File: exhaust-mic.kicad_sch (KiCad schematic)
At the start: 0 parts

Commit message: modified:   01-power.kicad_sch 	modified:   02-analog.kicad_sch 	modified:   03-adc.kicad_sch 	modified:   04-mcu.kicad_sch 	modified:   05-io.kicad_sch 	new file:   exhaust-mic.kicad_pro 	modified:   exhaust-mic.kicad_sch 	modified:   mic-head/mic-head.kicad_pcb 	modified:   mic-head/mic-head.kicad_pro 	modified:   mic-head/mic-head.kicad_sch
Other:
- company: Hayabusa / exhaust-mic -> (none)
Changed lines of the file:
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@@
 		(title "Exhaust-Mic - Stereo-Tonaufnahme Motor und Auspuff")
 		(date "2026-08-28")
-		(rev "A")
-		(company "Hayabusa / exhaust-mic")
+		(rev "1")
 	)
 	(text "Auslegung, Rauschbudget und Pegelplan:"

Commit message: Layout verdrahten, ERC/DRC bereinigen, Werkzeugkette auf KiCad 10
Mikrofonkopf ist fertig verdrahtet (0 offene Verbindungen, 0 DRC-Fehler).
Auf der Hauptplatine bleiben 16 Verbindungen offen, ebenfalls ohne
DRC-Fehler; sie sind im interaktiven Router von KiCad zu schliessen.

Schaltplan
- 3 Speisepin-Fehler behoben (+4V6, ADC-AVDD, Uhrenbatterie brauchen ein
  Speiseflag - sie werden ueber Drossel, Ferrit bzw. Zelle gespeist und
  haben damit keine Quelle im Sinne der Regelpruefung)
- Netzname GND_CHASSIS entfernt: lag auf demselben Knoten wie GND
- TLV1117LV33 hatte einen Pin 4 fuer die Kuehlfahne, den es im Footprint
  SOT-223-3_TabPin2 nicht gibt - dort traegt Pad 2 die Fahne
- Piezo von Durchsteck- auf SMD-Ausfuehrung (Murata PKMCS0909E): fuer den
  12,5-mm-Typ gibt es keine Position, an der seine Anschluesse nicht auf
  der Gegenseite auf Pads treffen
- ERC laeuft jetzt fehlerfrei

Layout
- Durchsteckpads belegen beide Seiten. J1, J4 und J6 standen ueber
  rueckseitigen Bauteilen; das waren vier echte Kurzschluesse, unter
  anderem GPS_PPS gegen Masse an der Knopfzelle. Die eigene Pruefung
  vergleicht Durchsteckpads jetzt gegen beide Seiten, pad-genau
- In2 traegt keine Versorgungsinseln mehr, sondern Signale. Vorher wich
  der Autorouter auf die Masseflaeche aus - 140 Segmente aus 30 Netzen
  quer durch In1. Der DSN-Export kennzeichnet In1 nun als Versorgungslage
- Masseflaechen auf den Aussenlagen mit Naehvias an In1 angebunden und auf
  automatische Inselentfernung gestellt
- Netzklasse auf 0,18 mm Bahn, 0,15 mm Abstand, 0,5/0,25-mm-Via verengt;
  mit KiCads Vorgabewerten blieb rund ein Dutzend Verbindungen mehr offen
- Beschaffungsfelder unsichtbar und auf die Fab-Lage: sichtbar im
  Siebdruck ueberdecken die Herstellernummern die halbe Platine, das
  waren 151 der urspruenglich 214 Regelwarnungen

Werkzeuge
- pipeline.sh fasst den Layoutlauf zusammen
- fix_drc.py nimmt KiCads Regelpruefung als Instanz und entfernt, was sie
  beanstandet - die eigenen Abst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
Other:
- company: (none) -> Hayabusa / exhaust-mic
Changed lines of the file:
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@@
 		(title "Exhaust-Mic - Stereo-Tonaufnahme Motor und Auspuff")
 		(date "2026-08-28")
-		(rev "1")
+		(rev "A")
+		(company "Hayabusa / exhaust-mic")
 	)
 	(text "Auslegung, Rauschbudget und Pegelplan:"
@@
 		)
 	)
-	(embedded_fonts no)
 )

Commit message: modified:   01-power.kicad_sch 	modified:   02-analog.kicad_sch 	modified:   03-adc.kicad_sch 	modified:   04-mcu.kicad_sch 	modified:   05-io.kicad_sch 	modified:   exhaust-mic.kicad_pcb 	modified:   exhaust-mic.kicad_pro 	modified:   exhaust-mic.kicad_sch 	modified:   mic-head/mic-head.kicad_pcb 	modified:   mic-head/mic-head.kicad_pro 	modified:   mic-head/mic-head.kicad_sch 	new file:   ~exhaust-mic.kicad_pro.lck
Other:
- company: Hayabusa / exhaust-mic -> (none)
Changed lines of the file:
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@@
 		(title "Exhaust-Mic - Stereo-Tonaufnahme Motor und Auspuff")
 		(date "2026-08-28")
-		(rev "A")
-		(company "Hayabusa / exhaust-mic")
+		(rev "1")
 	)
 	(text "Auslegung, Rauschbudget und Pegelplan:"
@@
 		)
 	)
+	(embedded_fonts no)
 )

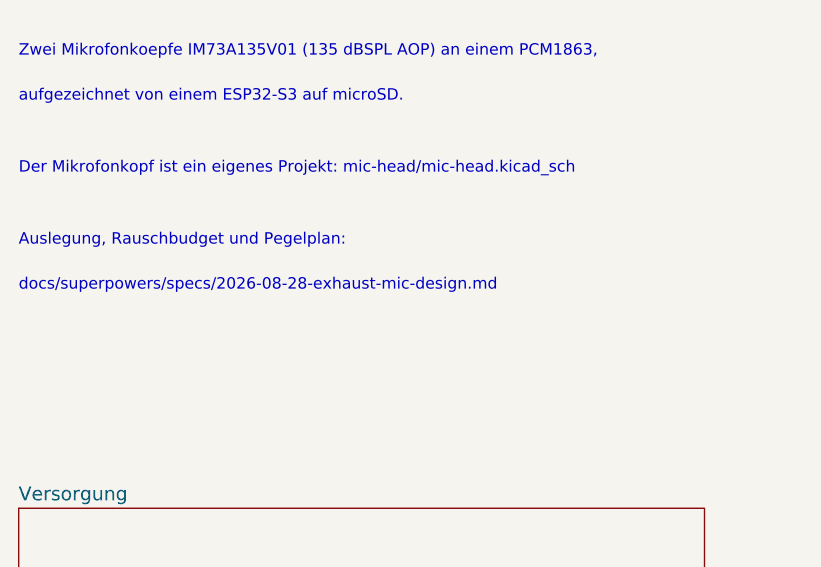
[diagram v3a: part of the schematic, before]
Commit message: Verweise auf die Spezifikation auf docs/specs umstellen
Der Pfad enthielt ein Verzeichnis, dessen Name nichts mit dem Projekt zu
tun hat. Er stand an sechs Stellen, darunter als Text auf dem
Schaltplanblatt selbst - die beiden Schaltplan-PDF sind deshalb neu
erzeugt.
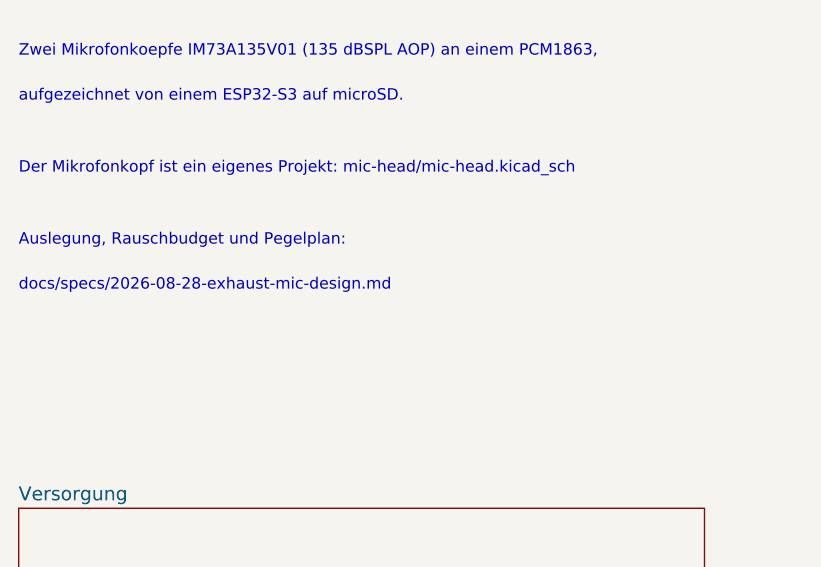
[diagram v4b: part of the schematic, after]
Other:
- note added: "docs/specs/2026-08-28-exhaust-mic-design.md"
- note removed: "docs/superpowers/specs/2026-08-28-exhaust-mic-design.md"
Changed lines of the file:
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@@
 		)
 	)
-	(text "docs/superpowers/specs/2026-08-28-exhaust-mic-design.md"
+	(text "docs/specs/2026-08-28-exhaust-mic-design.md"
 		(exclude_from_sim no)
 		(at 30 86 0)
